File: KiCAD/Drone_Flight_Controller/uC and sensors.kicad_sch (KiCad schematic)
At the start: 5 parts

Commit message: Solve Errors
Solve Errors
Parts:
- gave numbers to parts that had none: 5
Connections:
- no-connect marks 10 -> 9
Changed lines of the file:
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@@
-	)
-	(no_connect
-		(at 392.43 69.85)
 	)
 	(no_connect
@@
 	)
 	(label "IO23"
-		(at 210.82 104.14 180)
+		(at 209.55 104.14 180)
 		(effects
 			(font
@@
 	)
 	(label "IO27"
-		(at 205.74 111.76 180)
+		(at 204.47 111.76 180)
 		(effects
 			(font
@@
 	)
 	(label "IO21"
-		(at 210.82 99.06 180)
+		(at 209.55 99.06 180)
 		(effects
 			(font
@@
 	)
 	(label "Motor3"
-		(at 213.36 83.82 180)
+		(at 212.09 83.82 180)
 		(effects
 			(font
@@
 	)
 	(label "Motor1"
-		(at 213.36 78.74 180)
+		(at 212.09 78.74 180)
 		(effects
 			(font
@@
 	)
 	(label "Motor2"
-		(at 213.36 81.28 180)
+		(at 212.09 81.28 180)
 		(effects
 			(font
@@
 	)
 	(label "IO22"
-		(at 210.82 101.6 180)
+		(at 209.55 101.6 180)
 		(effects
 			(font
@@
 	)
 	(label "IO19"
-		(at 218.44 96.52 180)
+		(at 217.17 96.52 180)
 		(effects
 			(font
@@
 	)
 	(label "IO16"
-		(at 218.44 88.9 180)
+		(at 217.17 88.9 180)
 		(effects
 			(font
@@
 	)
 	(label "IO26"
-		(at 205.74 109.22 180)
+		(at 204.47 109.22 180)
 		(effects
 			(font
@@
 	)
 	(label "IO18"
-		(at 218.44 93.98 180)
+		(at 217.17 93.98 180)
 		(effects
 			(font
@@
 	)
 	(label "IO25"
-		(at 205.74 106.68 180)
+		(at 204.47 106.68 180)
 		(effects
 			(font
@@
 	)
 	(label "Motor4"
-		(at 213.36 86.36 180)
+		(at 212.09 86.36 180)
 		(effects
 			(font
@@
 	)
 	(label "IO17"
-		(at 218.44 91.44 180)
+		(at 217.17 91.44 180)
 		(effects
 			(font
@@
 		(dnp no)
 		(fields_autoplaced yes)
-		(property "Reference" "U?"
+		(property "Reference" "U23"
 			(at 179.9433 55.88 0)
 			(effects
@@
 			(project "Drone_Flight_Controller"
 				(path "/05daaa24-e506-4b9a-9564-8bf799413ca8/be1bc5c9-9814-4f01-a307-b935c6145e5a"
-					(reference "U?")
+					(reference "U23")
 					(unit 1)
 				)
@@
 		(dnp no)
 		(fields_autoplaced yes)
-		(property "Reference" "#PWR?"
+		(property "Reference" "#PWR0103"
 			(at 124.46 140.97 0)
 			(effects
@@
 			(project "Drone_Flight_Controller"
 				(path "/05daaa24-e506-4b9a-9564-8bf799413ca8/be1bc5c9-9814-4f01-a307-b935c6145e5a"
-					(reference "#PWR?")
+					(reference "#PWR0103")
+					(unit 1)
+				)
+			)
+		)
+	)
+	(symbol
+		(lib_id "power:+3.3V")
+		(at 124.46 88.9 0)
+		(unit 1)
+		(exclude_from_sim no)
+		(in_bom yes)
+		(on_board yes)
+		(dnp no)
+		(fields_autoplaced yes)
+		(property "Reference" "#PWR012"
+			(at 124.46 92.71 0)
+			(effects
+				(font
+					(size 1.27 1.27)
+				)
+				(hide yes)
+			)
+		)
+		(property "Value" "+3.3V"
+			(at 124.46 83.82 0)
+			(effects
+				(font
+					(size 1.27 1.27)
+				)
+			)
+		)
+		(property "Footprint" ""
+			(at 124.46 88.9 0)
+			(effects
+				(font
+					(size 1.27 1.27)
+				)
+				(hide yes)
+			)
+		)
+		(property "Datasheet" ""
+			(at 124.46 88.9 0)
+			(effects
+				(font
+					(size 1.27 1.27)
+				)
+				(hide yes)
+			)
+		)
+		(property "Description" "Power symbol creates a global label with name \"+3.3V\""
+			(at 124.46 88.9 0)
+			(effects
+				(font
+					(size 1.27 1.27)
+				)
+				(hide yes)
+			)
+		)
+		(pin "1"
+		)
+		(instances
+			(project ""
+				(path "/05daaa24-e506-4b9a-9564-8bf799413ca8/be1bc5c9-9814-4f01-a307-b935c6145e5a"
+					(reference "#PWR012")
 					(unit 1)
 				)
@@
 		(dnp no)
 		(fields_autoplaced yes)
-		(property "Reference" "#PWR?"
+		(property "Reference" "#PWR0101"
 			(at 177.8 138.43 0)
 			(effects
@@
 			(project "Drone_Flight_Controller"
 				(path "/05daaa24-e506-4b9a-9564-8bf799413ca8/be1bc5c9-9814-4f01-a307-b935c6145e5a"
-					(reference "#PWR?")
+					(reference "#PWR0101")
 					(unit 1)
 				)
@@
 		(dnp no)
 		(fields_autoplaced yes)
-		(property "Reference" "U?"
+		(property "Reference" "U22"
 			(at 131.6833 91.44 0)
 			(effects
@@
 			(project "Drone_Flight_Controller"
 				(path "/05daaa24-e506-4b9a-9564-8bf799413ca8/be1bc5c9-9814-4f01-a307-b935c6145e5a"
-					(reference "U?")
+					(reference "U22")
 					(unit 1)
 				)
@@
 		(dnp no)
 		(fields_autoplaced yes)
-		(property "Reference" "C?"
+		(property "Reference" "C21"
 			(at 158.75 109.2199 0)
 			(effects
@@
 			(project "Drone_Flight_Controller"
 				(path "/05daaa24-e506-4b9a-9564-8bf799413ca8/be1bc5c9-9814-4f01-a307-b935c6145e5a"
-					(reference "C?")
-					(unit 1)
-				)
-			)
-		)
-	)
-	(symbol
-		(lib_id "power:+3.3V")
-		(at 124.46 88.9 0)
-		(unit 1)
-		(exclude_from_sim no)
-		(in_bom yes)
-		(on_board yes)
-		(dnp no)
-		(fields_autoplaced yes)
-		(property "Reference" "#PWR?"
-			(at 124.46 92.71 0)
-			(effects
-				(font
-					(size 1.27 1.27)
-				)
-				(hide yes)
-			)
-		)
-		(property "Value" "+3.3V"
-			(at 124.46 83.82 0)
-			(effects
-				(font
-					(size 1.27 1.27)
-				)
-			)
-		)
-		(property "Footprint" ""
-			(at 124.46 88.9 0)
-			(effects
-				(font
-					(size 1.27 1.27)
-				)
-				(hide yes)
-			)
-		)
-		(property "Datasheet" ""
-			(at 124.46 88.9 0)
-			(effects
-				(font
-					(size 1.27 1.27)
-				)
-				(hide yes)
-			)
-		)
-		(property "Description" "Power symbol creates a global label with name \"+3.3V\""
-			(at 124.46 88.9 0)
-			(effects
-				(font
-					(size 1.27 1.27)
-				)
-				(hide yes)
-			)
-		)
-		(pin "1"
-		)
-		(instances
-			(project "Drone_Flight_Controller"
-				(path "/05daaa24-e506-4b9a-9564-8bf799413ca8/be1bc5c9-9814-4f01-a307-b935c6145e5a"
-					(reference "#PWR?")
+					(reference "C21")
 					(unit 1)
 				)
@@
 		(dnp no)
 		(fields_autoplaced yes)
-		(property "Reference" "#PWR?"
+		(property "Reference" "#PWR0102"
 			(at 177.8 57.15 0)
 			(effects
@@
 			(project "Drone_Flight_Controller"
 				(path "/05daaa24-e506-4b9a-9564-8bf799413ca8/be1bc5c9-9814-4f01-a307-b935c6145e5a"
-					(reference "#PWR?")
+					(reference "#PWR0102")
 					(unit 1)
 				)
@@
 		(dnp no)
 		(fields_autoplaced yes)
-		(property "Reference" "U?"
+		(property "Reference" "U21"
 			(at 102.87 114.2298 0)
 			(effects
@@
 			(project "Drone_Flight_Controller"
 				(path "/05daaa24-e506-4b9a-9564-8bf799413ca8/be1bc5c9-9814-4f01-a307-b935c6145e5a"
-					(reference "U?")
+					(reference "U21")
 					(unit 1)
 				)
@@
 		(dnp no)
 		(fields_autoplaced yes)
-		(property "Reference" "#PWR?"
+		(property "Reference" "#PWR0105"
 			(at 91.44 110.49 0)
 			(effects
@@
 			(project "Drone_Flight_Controller"
 				(path "/05daaa24-e506-4b9a-9564-8bf799413ca8/be1bc5c9-9814-4f01-a307-b935c6145e5a"
-					(reference "#PWR?")
+					(reference "#PWR0105")
 					(unit 1)
 				)
@@
 		(dnp no)
 		(fields_autoplaced yes)
-		(property "Reference" "C?"
+		(property "Reference" "C22"
 			(at 148.59 116.84 90)
 			(effects
@@
 			(project "Drone_Flight_Controller"
 				(path "/05daaa24-e506-4b9a-9564-8bf799413ca8/be1bc5c9-9814-4f01-a307-b935c6145e5a"
-					(reference "C?")
+					(reference "C22")
 					(unit 1)
 				)
@@
 		(dnp no)
 		(fields_autoplaced yes)
-		(property "Reference" "#PWR?"
+		(property "Reference" "#PWR0106"
 			(at 88.9 138.43 0)
 			(effects
@@
 			(project "Drone_Flight_Controller"
 				(path "/05daaa24-e506-4b9a-9564-8bf799413ca8/be1bc5c9-9814-4f01-a307-b935c6145e5a"
-					(reference "#PWR?")
+					(reference "#PWR0106")
 					(unit 1)
 				)

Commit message: Add Programming
Add Programming
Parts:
- added R17: 10k, Resistor_SMD:R_0805_2012Metric_Pad1.20x1.40mm_HandSolder, symbol Device:R
- C21: footprint (none) -> Capacitor_SMD:C_0805_2012Metric_Pad1.18x1.45mm_HandSolder; Link (none) -> https://www.mouser.at/ProductDetail/Vishay-Vitramon/VJ0805Y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
- C22: footprint (none) -> Capacitor_SMD:C_0805_2012Metric_Pad1.18x1.45mm_HandSolder; Link (none) -> https://www.mouser.at/ProductDetail/Samsung-Electro-Mechani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
- U21: footprint (none) -> Package_LGA:Bosch_LGA-8_2x2.5mm_P0.65mm_ClockwisePinNumbering
- U23: Link (none) -> /
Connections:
- net IO26 is gone; now on net Buzzer: U23.11 (IO26)
- net +3.3V: now also R17.2
- net Buzzer: no longer U23.29 (IO5)
- net at U23.17 (SHD/SD2): now also U22.19 (COM1)
- net at U23.18 (SWP/SD3): now also U22.20 (COM0)
- net at U23.19 (SCS/CMD): now also U21.4 (SCK)
- net at U23.20 (SCK/CLK): no longer U21.4 (SCK)
- net at U23.21 (SDO/SD0): no longer U21.5 (SDO)
- net at U23.22 (SDI/SD1): now also U21.5 (SDO); no longer U21.3 (SDI)
- net at U21.2 (~{CS}): now also U23.29 (IO5); no longer U23.25 (IO0)
- net at U22.4 (~{BOOT_LOAD_PIN}), U23.26 (IO4): now also R17.1
- net Programming TX: now reaches U23.34 (RXD0/IO3)
- net Programming TX: no longer U22.20 (COM0)
- net Programming RX: now reaches U23.35 (TXD0/IO1)
- net Programming RX: no longer U22.19 (COM1)
- net CC1: no longer names the net of U23.8 (IO32)
- net CC2: no longer names the net of U23.9 (IO33)
- net D+: no longer names the net of U23.7 (IO35)
- net D-: no longer names the net of U23.6 (IO34)
- net IO16 renamed GPS RX
- net IO17 renamed GPS TX
- net IO18: no longer names the net of U23.30 (IO18)
- net IO19 renamed Programming CTS
- net IO21: no longer names the net of U23.33 (IO21)
- net IO22 renamed Programming RTS
- net IO23: no longer names the net of U23.37 (IO23)
- net IO23: now also U21.3 (SDI)
- net IO25 renamed BATT Monitor
- net IO27: no longer names the net of U23.12 (IO27)
- new net ~{Programming}: U23.25 (IO0)
- no-connect marks 9 -> 15
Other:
- moved on the sheet: U21, U23

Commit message: Reanotate
Reanotate
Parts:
- renumbered C22 to C401, C21 to C402, R17 to R401, U21 to U401, U22 to U402, U23 to U403
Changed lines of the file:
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@@
 		(on_board yes)
 		(dnp no)
-		(property "Reference" "U23"
+		(property "Reference" "U403"
 			(at 193.548 89.662 90)
 			(effects
@@
 			(project "Drone_Flight_Controller"
 				(path "/05daaa24-e506-4b9a-9564-8bf799413ca8/be1bc5c9-9814-4f01-a307-b935c6145e5a"
-					(reference "U23")
+					(reference "U403")
 					(unit 1)
 				)
@@
 		(dnp no)
 		(fields_autoplaced yes)
-		(property "Reference" "#PWR0103"
+		(property "Reference" "#PWR0404"
 			(at 124.46 140.97 0)
 			(effects
@@
 			(project "Drone_Flight_Controller"
 				(path "/05daaa24-e506-4b9a-9564-8bf799413ca8/be1bc5c9-9814-4f01-a307-b935c6145e5a"
-					(reference "#PWR0103")
+					(reference "#PWR0404")
 					(unit 1)
 				)
@@
 		(dnp no)
 		(fields_autoplaced yes)
-		(property "Reference" "#PWR0104"
+		(property "Reference" "#PWR0403"
 			(at 124.46 92.71 0)
 			(effects
@@
 			(project ""
 				(path "/05daaa24-e506-4b9a-9564-8bf799413ca8/be1bc5c9-9814-4f01-a307-b935c6145e5a"
-					(reference "#PWR0104")
+					(reference "#PWR0403")
 					(unit 1)
 				)
@@
 		(dnp no)
 		(fields_autoplaced yes)
-		(property "Reference" "#PWR0101"
+		(property "Reference" "#PWR0406"
 			(at 209.55 138.43 0)
 			(effects
@@
 			(project "Drone_Flight_Controller"
 				(path "/05daaa24-e506-4b9a-9564-8bf799413ca8/be1bc5c9-9814-4f01-a307-b935c6145e5a"
-					(reference "#PWR0101")
+					(reference "#PWR0406")
 					(unit 1)
 				)
@@
 		(dnp no)
 		(fields_autoplaced yes)
-		(property "Reference" "U22"
+		(property "Reference" "U402"
 			(at 131.6833 91.44 0)
 			(effects
@@
 			(project "Drone_Flight_Controller"
 				(path "/05daaa24-e506-4b9a-9564-8bf799413ca8/be1bc5c9-9814-4f01-a307-b935c6145e5a"
-					(reference "U22")
+					(reference "U402")
 					(unit 1)
 				)
@@
 		(dnp no)
 		(fields_autoplaced yes)
-		(property "Reference" "C21"
+		(property "Reference" "C402"
 			(at 158.75 109.2199 0)
 			(effects
@@
 			(project "Drone_Flight_Controller"
 				(path "/05daaa24-e506-4b9a-9564-8bf799413ca8/be1bc5c9-9814-4f01-a307-b935c6145e5a"
-					(reference "C21")
+					(reference "C402")
 					(unit 1)
 				)
@@
 		(dnp no)
 		(fields_autoplaced yes)
-		(property "Reference" "R17"
+		(property "Reference" "R401"
 			(at 118.11 85.09 90)
 			(effects
@@
 			(project ""
 				(path "/05daaa24-e506-4b9a-9564-8bf799413ca8/be1bc5c9-9814-4f01-a307-b935c6145e5a"
-					(reference "R17")
+					(reference "R401")
 					(unit 1)
 				)
@@
 		(dnp no)
 		(fields_autoplaced yes)
-		(property "Reference" "#PWR0102"
+		(property "Reference" "#PWR0405"
 			(at 209.55 57.15 0)
 			(effects
@@
 			(project "Drone_Flight_Controller"
 				(path "/05daaa24-e506-4b9a-9564-8bf799413ca8/be1bc5c9-9814-4f01-a307-b935c6145e5a"
-					(reference "#PWR0102")
+					(reference "#PWR0405")
 					(unit 1)
 				)
@@
 		(on_board yes)
 		(dnp no)
-		(property "Reference" "U21"
+		(property "Reference" "U401"
 			(at 81.28 109.22 0)
 			(effects
@@
 			(project "Drone_Flight_Controller"
 				(path "/05daaa24-e506-4b9a-9564-8bf799413ca8/be1bc5c9-9814-4f01-a307-b935c6145e5a"
-					(reference "U21")
+					(reference "U401")
 					(unit 1)
 				)
@@
 		(dnp no)
 		(fields_autoplaced yes)
-		(property "Reference" "#PWR0105"
+		(property "Reference" "#PWR0402"
 			(at 74.93 110.49 0)
 			(effects
@@
 			(project "Drone_Flight_Controller"
 				(path "/05daaa24-e506-4b9a-9564-8bf799413ca8/be1bc5c9-9814-4f01-a307-b935c6145e5a"
-					(reference "#PWR0105")
+					(reference "#PWR0402")
 					(unit 1)
 				)
@@
 		(on_board yes)
 		(dnp no)
-		(property "Reference" "C22"
+		(property "Reference" "C401"
 			(at 148.59 121.158 90)
 			(effects
@@
 			(project "Drone_Flight_Controller"
 				(path "/05daaa24-e506-4b9a-9564-8bf799413ca8/be1bc5c9-9814-4f01-a307-b935c6145e5a"
-					(reference "C22")
+					(reference "C401")
 					(unit 1)
 				)
@@
 		(dnp no)
 		(fields_autoplaced yes)
-		(property "Reference" "#PWR0106"
+		(property "Reference" "#PWR0401"
 			(at 72.39 138.43 0)
 			(effects
@@
 			(project "Drone_Flight_Controller"
 				(path "/05daaa24-e506-4b9a-9564-8bf799413ca8/be1bc5c9-9814-4f01-a307-b935c6145e5a"
-					(reference "#PWR0106")
-					(unit 1)
-				)
+					(reference "#PWR0401")
+					(unit 1)
+				)

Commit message: Reannotate
Reannotate
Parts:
- renumbered C402 to C401, C401 to C402, U403 to U401, U401 to U402, U402 to U403
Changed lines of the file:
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@@
 		(on_board yes)
 		(dnp no)
-		(property "Reference" "U403"
+		(property "Reference" "U401"
 			(at 193.548 89.662 90)
 			(effects
@@
 			(project "Drone_Flight_Controller"
 				(path "/05daaa24-e506-4b9a-9564-8bf799413ca8/be1bc5c9-9814-4f01-a307-b935c6145e5a"
-					(reference "U403")
+					(reference "U401")
 					(unit 1)
 				)
@@
 		(dnp no)
 		(fields_autoplaced yes)
-		(property "Reference" "#PWR0404"
+		(property "Reference" "#PWR0406"
 			(at 124.46 140.97 0)
 			(effects
@@
 			(project "Drone_Flight_Controller"
 				(path "/05daaa24-e506-4b9a-9564-8bf799413ca8/be1bc5c9-9814-4f01-a307-b935c6145e5a"
-					(reference "#PWR0404")
+					(reference "#PWR0406")
 					(unit 1)
 				)
@@
 		(dnp no)
 		(fields_autoplaced yes)
-		(property "Reference" "#PWR0403"
+		(property "Reference" "#PWR0402"
 			(at 124.46 92.71 0)
 			(effects
@@
 			(project ""
 				(path "/05daaa24-e506-4b9a-9564-8bf799413ca8/be1bc5c9-9814-4f01-a307-b935c6145e5a"
-					(reference "#PWR0403")
+					(reference "#PWR0402")
 					(unit 1)
 				)
@@
 		(dnp no)
 		(fields_autoplaced yes)
-		(property "Reference" "#PWR0406"
+		(property "Reference" "#PWR0405"
 			(at 209.55 138.43 0)
 			(effects
@@
 			(project "Drone_Flight_Controller"
 				(path "/05daaa24-e506-4b9a-9564-8bf799413ca8/be1bc5c9-9814-4f01-a307-b935c6145e5a"
-					(reference "#PWR0406")
+					(reference "#PWR0405")
 					(unit 1)
 				)
@@
 		(dnp no)
 		(fields_autoplaced yes)
-		(property "Reference" "U402"
+		(property "Reference" "U403"
 			(at 131.6833 91.44 0)
 			(effects
@@
 			(project "Drone_Flight_Controller"
 				(path "/05daaa24-e506-4b9a-9564-8bf799413ca8/be1bc5c9-9814-4f01-a307-b935c6145e5a"
-					(reference "U402")
+					(reference "U403")
 					(unit 1)
 				)
@@
 		(dnp no)
 		(fields_autoplaced yes)
-		(property "Reference" "C402"
+		(property "Reference" "C401"
 			(at 158.75 109.2199 0)
 			(effects
@@
 			(project "Drone_Flight_Controller"
 				(path "/05daaa24-e506-4b9a-9564-8bf799413ca8/be1bc5c9-9814-4f01-a307-b935c6145e5a"
-					(reference "C402")
+					(reference "C401")
 					(unit 1)
 				)
@@
 		(dnp no)
 		(fields_autoplaced yes)
-		(property "Reference" "#PWR0405"
+		(property "Reference" "#PWR0401"
 			(at 209.55 57.15 0)
 			(effects
@@
 			(project "Drone_Flight_Controller"
 				(path "/05daaa24-e506-4b9a-9564-8bf799413ca8/be1bc5c9-9814-4f01-a307-b935c6145e5a"
-					(reference "#PWR0405")
+					(reference "#PWR0401")
 					(unit 1)
 				)
@@
 		(on_board yes)
 		(dnp no)
-		(property "Reference" "U401"
+		(property "Reference" "U402"
 			(at 81.28 109.22 0)
 			(effects
@@
 			(project "Drone_Flight_Controller"
 				(path "/05daaa24-e506-4b9a-9564-8bf799413ca8/be1bc5c9-9814-4f01-a307-b935c6145e5a"
-					(reference "U401")
+					(reference "U402")
 					(unit 1)
 				)
@@
 		(dnp no)
 		(fields_autoplaced yes)
-		(property "Reference" "#PWR0402"
+		(property "Reference" "#PWR0403"
 			(at 74.93 110.49 0)
 			(effects
@@
 			(project "Drone_Flight_Controller"
 				(path "/05daaa24-e506-4b9a-9564-8bf799413ca8/be1bc5c9-9814-4f01-a307-b935c6145e5a"
-					(reference "#PWR0402")
+					(reference "#PWR0403")
 					(unit 1)
 				)
@@
 		(on_board yes)
 		(dnp no)
-		(property "Reference" "C401"
+		(property "Reference" "C402"
 			(at 148.59 121.158 90)
 			(effects
@@
 			(project "Drone_Flight_Controller"
 				(path "/05daaa24-e506-4b9a-9564-8bf799413ca8/be1bc5c9-9814-4f01-a307-b935c6145e5a"
-					(reference "C401")
+					(reference "C402")
 					(unit 1)
 				)
@@
 		(dnp no)
 		(fields_autoplaced yes)
-		(property "Reference" "#PWR0401"
+		(property "Reference" "#PWR0404"
 			(at 72.39 138.43 0)
 			(effects
@@
 			(project "Drone_Flight_Controller"
 				(path "/05daaa24-e506-4b9a-9564-8bf799413ca8/be1bc5c9-9814-4f01-a307-b935c6145e5a"
-					(reference "#PWR0401")
-					(unit 1)
-				)
+					(reference "#PWR0404")
+					(unit 1)
+				)

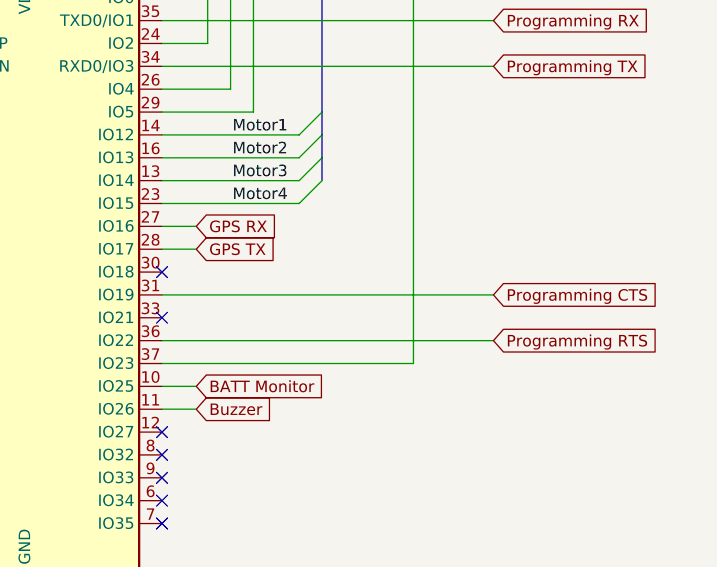
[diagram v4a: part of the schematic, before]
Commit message: Fix GPS RX/TX mixup
Fix GPS RX/TX mixup
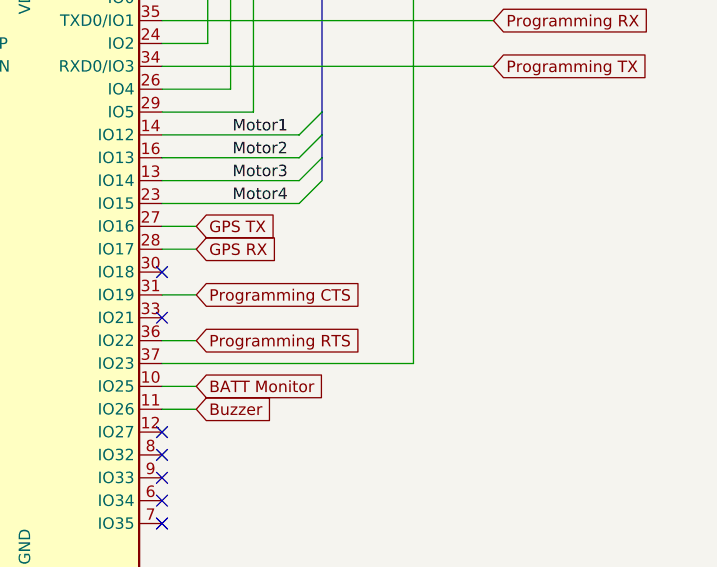
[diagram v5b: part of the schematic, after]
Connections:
- net GPS RX: now also U401.28 (IO17); no longer U401.27 (IO16)
- net GPS TX: now also U401.27 (IO16); no longer U401.28 (IO17)
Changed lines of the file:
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@@
 	(title_block
 		(title "uC and sensors")
-		(date "2025-07-13")
+		(date "2025-07-17")
 		(rev "V1")
 		(company "HTL Steyr")
@@
 	(wire
 		(pts
-			(xy 224.79 96.52) (xy 261.62 96.52)
+			(xy 224.79 96.52) (xy 228.6 96.52)
 		)
 		(stroke
@@
 	(wire
 		(pts
-			(xy 224.79 101.6) (xy 261.62 101.6)
+			(xy 224.79 101.6) (xy 228.6 101.6)
 		)
 		(stroke
@@
 	(global_label "Programming CTS"
 		(shape input)
-		(at 261.62 96.52 0)
+		(at 228.6 96.52 0)
 		(fields_autoplaced yes)
 		(effects
@@
 		)
 		(property "Intersheetrefs" "${INTERSHEET_REFS}"
-			(at 281.5987 96.52 0)
+			(at 248.5787 96.52 0)
 			(effects
 				(font
@@
 		)
 	)
-	(global_label "GPS RX"
-		(shape input)
-		(at 228.6 88.9 0)
-		(fields_autoplaced yes)
-		(effects
-			(font
-				(size 1.27 1.27)
-			)
-			(justify left)
-		)
-		(property "Intersheetrefs" "${INTERSHEET_REFS}"
-			(at 238.7818 88.9 0)
-			(effects
-				(font
-					(size 1.27 1.27)
-				)
-				(justify left)
-				(hide yes)
-			)
-		)
-	)
 	(global_label "Motor[1..4]"
 		(shape input)
@@
 		)
 	)
+	(global_label "GPS TX"
+		(shape input)
+		(at 228.6 88.9 0)
+		(fields_autoplaced yes)
+		(effects
+			(font
+				(size 1.27 1.27)
+			)
+			(justify left)
+		)
+		(property "Intersheetrefs" "${INTERSHEET_REFS}"
+			(at 238.4794 88.9 0)
+			(effects
+				(font
+					(size 1.27 1.27)
+				)
+				(justify left)
+				(hide yes)
+			)
+		)
+	)
 	(global_label "Buzzer"
 		(shape input)
@@
 		)
 	)
+	(global_label "GPS RX"
+		(shape input)
+		(at 228.6 91.44 0)
+		(fields_autoplaced yes)
+		(effects
+			(font
+				(size 1.27 1.27)
+			)
+			(justify left)
+		)
+		(property "Intersheetrefs" "${INTERSHEET_REFS}"
+			(at 238.7818 91.44 0)
+			(effects
+				(font
+					(size 1.27 1.27)
+				)
+				(justify left)
+				(hide yes)
+			)
+		)
+	)
 	(global_label "~{Programming}"
 		(shape input)
@@
 		)
 	)
-	(global_label "GPS TX"
+	(global_label "Programming RTS"
 		(shape input)
-		(at 228.6 91.44 0)
+		(at 228.6 101.6 0)
 		(fields_autoplaced yes)
 		(effects
@@
 		)
 		(property "Intersheetrefs" "${INTERSHEET_REFS}"
-			(at 238.4794 91.44 0)
+			(at 248.5787 101.6 0)
 			(effects
 				(font
-					(size 1.27 1.27)
-				)
-				(justify left)
-				(hide yes)
-			)
-		)
-	)
-	(global_label "Programming RTS"
-		(shape input)
-		(at 261.62 101.6 0)
-		(fields_autoplaced yes)
-		(effects
-			(font
-				(size 1.27 1.27)
-			)
-			(justify left)
-		)
-		(property "Intersheetrefs" "${INTERSHEET_REFS}"
-			(at 281.5987 101.6 0)
-			(effects
-				(font

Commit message: Export BOM
Export BOM
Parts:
- U401: Link / -> https://www.mouser.at/ProductDetail/Espressif-Systems/ESP32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
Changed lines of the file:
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@@
 			)
 		)
-		(property "Datasheet" "https://www.espressif.com/sites/default/files/documentation/esp32-wroom-32_datasheet_en.pdf"
+		(property "Datasheet" "https://www.mouser.at/datasheet/2/891/esp32_wroom_32e_esp32_wroom_32ue_datasheet_en-1855879.pdf"
 			(at 201.93 92.71 0)
 			(effects
@@
 			)
 		)
-		(property "Link" "/"
+		(property "Link" "https://www.mouser.at/ProductDetail/Espressif-Systems/ESP32-WROOM-32E-N8?qs=Li%252BoUPsLEnsLnZW%252BGLgUhw%3D%3D"
 			(at 209.55 93.98 90)
 			(effects
